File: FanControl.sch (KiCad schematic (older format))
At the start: 4 parts

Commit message: Finish the schematics. All pins are assinged to the NUCLEO-64 board.
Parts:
- gave numbers to parts that had none: 4
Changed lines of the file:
@@
 $EndDescr
 $Comp
-L Device:R R?
+L Device:R R51
 U 1 1 5AB90282
 P 4500 3500
-AR Path="/5AB9002A/5AB90282" Ref="R?"  Part="1"
-AR Path="/5AB91A71/5AB90282" Ref="R?"  Part="1"
-F 0 "R?" V 4293 3500 50  0000 C CNN
+AR Path="/5AB9002A/5AB90282" Ref="R51"  Part="1"
+AR Path="/5AB91A5D/5AB90282" Ref="R53"  Part="1"
+AR Path="/5AB91A68/5AB90282" Ref="R55"  Part="1"
+AR Path="/5AB91A71/5AB90282" Ref="R57"  Part="1"
+F 0 "R57" V 4293 3500 50  0000 C CNN
 F 1 "1k" V 4384 3500 50  0000 C CNN
 F 2 "" V 4430 3500 50  0001 C CNN
@@
 $EndComp
 $Comp
-L power:GND #PWR?
+L power:GND #PWR071
 U 1 1 5AB906E9
 P 5250 4000
-AR Path="/5AB9002A/5AB906E9" Ref="#PWR?"  Part="1"
-AR Path="/5AB91A71/5AB906E9" Ref="#PWR?"  Part="1"
-F 0 "#PWR?" H 5250 3750 50  0001 C CNN
+AR Path="/5AB9002A/5AB906E9" Ref="#PWR071"  Part="1"
+AR Path="/5AB91A5D/5AB906E9" Ref="#PWR072"  Part="1"
+AR Path="/5AB91A68/5AB906E9" Ref="#PWR073"  Part="1"
+AR Path="/5AB91A71/5AB906E9" Ref="#PWR074"  Part="1"
+F 0 "#PWR074" H 5250 3750 50  0001 C CNN
 F 1 "GND" H 5255 3827 50  0000 C CNN
 F 2 "" H 5250 4000 50  0001 C CNN
@@
 V_FAN
 $Comp
-L bsh105:BSH105 TR?
+L bsh105:BSH105 TR4
 U 1 1 5AB90621
 P 5100 3500
-AR Path="/5AB9002A/5AB90621" Ref="TR?"  Part="1"
-AR Path="/5AB91A71/5AB90621" Ref="TR?"  Part="1"
-F 0 "TR?" H 5328 3553 70  0000 L CNN
+AR Path="/5AB9002A/5AB90621" Ref="TR4"  Part="1"
+AR Path="/5AB91A5D/5AB90621" Ref="TR5"  Part="1"
+AR Path="/5AB91A68/5AB90621" Ref="TR6"  Part="1"
+AR Path="/5AB91A71/5AB90621" Ref="TR7"  Part="1"
+F 0 "TR7" H 5328 3553 70  0000 L CNN
 F 1 "PMV40UN2" H 5328 3439 60  0000 L CNN
 F 2 "" H 5100 3500 60  0000 C CNN
@@
 	5250 2700 5250 3150
 $Comp
-L Device:R R?
+L Device:R R50
 U 1 1 5AB969B0
 P 4250 3750
-F 0 "R?" H 4320 3796 50  0000 L CNN
+AR Path="/5AB9002A/5AB969B0" Ref="R50"  Part="1"
+AR Path="/5AB91A5D/5AB969B0" Ref="R52"  Part="1"
+AR Path="/5AB91A68/5AB969B0" Ref="R54"  Part="1"
+AR Path="/5AB91A71/5AB969B0" Ref="R56"  Part="1"
+F 0 "R56" H 4320 3796 50  0000 L CNN
 F 1 "10k" H 4320 3705 50  0000 L CNN
 F 2 "" V 4180 3750 50  0001 C CNN
@@
 	5250 3950 5250 4000
 $Comp
-L Device:D D?
+L Device:D D12
 U 1 1 5AB96AD6
 P 5250 2450
-F 0 "D?" V 5204 2529 50  0000 L CNN
+AR Path="/5AB9002A/5AB96AD6" Ref="D12"  Part="1"
+AR Path="/5AB91A5D/5AB96AD6" Ref="D13"  Part="1"
+AR Path="/5AB91A68/5AB96AD6" Ref="D14"  Part="1"
+AR Path="/5AB91A71/5AB96AD6" Ref="D15"  Part="1"
+F 0 "D15" V 5204 2529 50  0000 L CNN
 F 1 "DO-219AB" V 5295 2529 50  0000 L CNN
 F 2 "" H 5250 2450 50  0001 C CNN

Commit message: Split the bed heater in separate schematics.
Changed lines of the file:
@@
 $Descr A4 11693 8268
 encoding utf-8
-Sheet 34 35
+Sheet 31 35
 Title ""
 Date ""
@@
 AR Path="/5AB91A68/5AB90282" Ref="R55"  Part="1"
 AR Path="/5AB91A71/5AB90282" Ref="R57"  Part="1"
-F 0 "R57" V 4293 3500 50  0000 C CNN
+F 0 "R51" V 4293 3500 50  0000 C CNN
 F 1 "1k" V 4384 3500 50  0000 C CNN
 F 2 "" V 4430 3500 50  0001 C CNN
@@
 AR Path="/5AB91A68/5AB90621" Ref="TR6"  Part="1"
 AR Path="/5AB91A71/5AB90621" Ref="TR7"  Part="1"
-F 0 "TR7" H 5328 3553 70  0000 L CNN
+F 0 "TR4" H 5328 3553 70  0000 L CNN
 F 1 "PMV40UN2" H 5328 3439 60  0000 L CNN
 F 2 "" H 5100 3500 60  0000 C CNN
@@
 AR Path="/5AB91A68/5AB969B0" Ref="R54"  Part="1"
 AR Path="/5AB91A71/5AB969B0" Ref="R56"  Part="1"
-F 0 "R56" H 4320 3796 50  0000 L CNN
+F 0 "R50" H 4320 3796 50  0000 L CNN
 F 1 "10k" H 4320 3705 50  0000 L CNN
 F 2 "" V 4180 3750 50  0001 C CNN
@@
 AR Path="/5AB91A68/5AB96AD6" Ref="D14"  Part="1"
 AR Path="/5AB91A71/5AB96AD6" Ref="D15"  Part="1"
-F 0 "D15" V 5204 2529 50  0000 L CNN
+F 0 "D12" V 5204 2529 50  0000 L CNN
 F 1 "DO-219AB" V 5295 2529 50  0000 L CNN
 F 2 "" H 5250 2450 50  0001 C CNN

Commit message: Assigned footprints for all components. Inductors are approximate size. MOSFETs dont agree with the footprints. Saved pcb netlist report as report.txt.
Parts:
- D12: footprint (none) -> Diode_SMD:D_SOD-323F
- R50, R51: footprint (none) -> Resistor_SMD:R_0603_1608Metric
- TR4: value PMV40UN2 -> SI2318CDS; footprint (none) -> Package_TO_SOT_SMD:SOT-23
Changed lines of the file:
@@
 AR Path="/5AB91A68/5AB90282" Ref="R55"  Part="1"
 AR Path="/5AB91A71/5AB90282" Ref="R57"  Part="1"
-F 0 "R51" V 4293 3500 50  0000 C CNN
+F 0 "R57" V 4293 3500 50  0000 C CNN
 F 1 "1k" V 4384 3500 50  0000 C CNN
-F 2 "" V 4430 3500 50  0001 C CNN
+F 2 "Resistor_SMD:R_0603_1608Metric" V 4430 3500 50  0001 C CNN
 F 3 "~" H 4500 3500 50  0001 C CNN
 	1    4500 3500
@@
 AR Path="/5AB91A68/5AB90621" Ref="TR6"  Part="1"
 AR Path="/5AB91A71/5AB90621" Ref="TR7"  Part="1"
-F 0 "TR4" H 5328 3553 70  0000 L CNN
-F 1 "PMV40UN2" H 5328 3439 60  0000 L CNN
-F 2 "" H 5100 3500 60  0000 C CNN
+F 0 "TR7" H 5328 3553 70  0000 L CNN
+F 1 "SI2318CDS" H 5328 3439 60  0000 L CNN
+F 2 "Package_TO_SOT_SMD:SOT-23" H 5100 3500 60  0001 C CNN
 F 3 "" H 5100 3500 60  0000 C CNN
 	1    5100 3500
@@
 AR Path="/5AB91A68/5AB969B0" Ref="R54"  Part="1"
 AR Path="/5AB91A71/5AB969B0" Ref="R56"  Part="1"
-F 0 "R50" H 4320 3796 50  0000 L CNN
+F 0 "R56" H 4320 3796 50  0000 L CNN
 F 1 "10k" H 4320 3705 50  0000 L CNN
-F 2 "" V 4180 3750 50  0001 C CNN
+F 2 "Resistor_SMD:R_0603_1608Metric" V 4180 3750 50  0001 C CNN
 F 3 "~" H 4250 3750 50  0001 C CNN
 	1    4250 3750
@@
 AR Path="/5AB91A68/5AB96AD6" Ref="D14"  Part="1"
 AR Path="/5AB91A71/5AB96AD6" Ref="D15"  Part="1"
-F 0 "D12" V 5204 2529 50  0000 L CNN
+F 0 "D15" V 5204 2529 50  0000 L CNN
 F 1 "DO-219AB" V 5295 2529 50  0000 L CNN
-F 2 "" H 5250 2450 50  0001 C CNN
+F 2 "Diode_SMD:D_SOD-323F" H 5250 2450 50  0001 C CNN
 F 3 "~" H 5250 2450 50  0001 C CNN
 	1    5250 2450

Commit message: Updated components. Removed power supply. Component layout on PCB.
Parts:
- TR4: footprint Package_TO_SOT_SMD:SOT-23 -> PrntrBoardV1:SOT-23
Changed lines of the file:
@@
 $Descr A4 11693 8268
 encoding utf-8
-Sheet 31 35
+Sheet 31 34
 Title ""
 Date ""
@@
 AR Path="/5AB91A68/5AB90282" Ref="R55"  Part="1"
 AR Path="/5AB91A71/5AB90282" Ref="R57"  Part="1"
-F 0 "R57" V 4293 3500 50  0000 C CNN
+F 0 "R51" V 4293 3500 50  0000 C CNN
 F 1 "1k" V 4384 3500 50  0000 C CNN
 F 2 "Resistor_SMD:R_0603_1608Metric" V 4430 3500 50  0001 C CNN
@@
 AR Path="/5AB91A68/5AB90621" Ref="TR6"  Part="1"
 AR Path="/5AB91A71/5AB90621" Ref="TR7"  Part="1"
-F 0 "TR7" H 5328 3553 70  0000 L CNN
+F 0 "TR4" H 5328 3553 70  0000 L CNN
 F 1 "SI2318CDS" H 5328 3439 60  0000 L CNN
-F 2 "Package_TO_SOT_SMD:SOT-23" H 5100 3500 60  0001 C CNN
+F 2 "PrntrBoardV1:SOT-23" H 5100 3500 60  0001 C CNN
 F 3 "" H 5100 3500 60  0000 C CNN
 	1    5100 3500
@@
 AR Path="/5AB91A68/5AB969B0" Ref="R54"  Part="1"
 AR Path="/5AB91A71/5AB969B0" Ref="R56"  Part="1"
-F 0 "R56" H 4320 3796 50  0000 L CNN
+F 0 "R50" H 4320 3796 50  0000 L CNN
 F 1 "10k" H 4320 3705 50  0000 L CNN
 F 2 "Resistor_SMD:R_0603_1608Metric" V 4180 3750 50  0001 C CNN
@@
 AR Path="/5AB91A68/5AB96AD6" Ref="D14"  Part="1"
 AR Path="/5AB91A71/5AB96AD6" Ref="D15"  Part="1"
-F 0 "D15" V 5204 2529 50  0000 L CNN
+F 0 "D12" V 5204 2529 50  0000 L CNN
 F 1 "DO-219AB" V 5295 2529 50  0000 L CNN
 F 2 "Diode_SMD:D_SOD-323F" H 5250 2450 50  0001 C CNN

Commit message: Routed most of the power traces.
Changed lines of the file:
@@
 AR Path="/5AB91A68/5AB90282" Ref="R55"  Part="1"
 AR Path="/5AB91A71/5AB90282" Ref="R57"  Part="1"
-F 0 "R51" V 4293 3500 50  0000 C CNN
+F 0 "R57" V 4293 3500 50  0000 C CNN
 F 1 "1k" V 4384 3500 50  0000 C CNN
 F 2 "Resistor_SMD:R_0603_1608Metric" V 4430 3500 50  0001 C CNN
@@
 AR Path="/5AB91A68/5AB90621" Ref="TR6"  Part="1"
 AR Path="/5AB91A71/5AB90621" Ref="TR7"  Part="1"
-F 0 "TR4" H 5328 3553 70  0000 L CNN
+F 0 "TR7" H 5328 3553 70  0000 L CNN
 F 1 "SI2318CDS" H 5328 3439 60  0000 L CNN
 F 2 "PrntrBoardV1:SOT-23" H 5100 3500 60  0001 C CNN
@@
 AR Path="/5AB91A68/5AB969B0" Ref="R54"  Part="1"
 AR Path="/5AB91A71/5AB969B0" Ref="R56"  Part="1"
-F 0 "R50" H 4320 3796 50  0000 L CNN
+F 0 "R56" H 4320 3796 50  0000 L CNN
 F 1 "10k" H 4320 3705 50  0000 L CNN
 F 2 "Resistor_SMD:R_0603_1608Metric" V 4180 3750 50  0001 C CNN
@@
 AR Path="/5AB91A68/5AB96AD6" Ref="D14"  Part="1"
 AR Path="/5AB91A71/5AB96AD6" Ref="D15"  Part="1"
-F 0 "D12" V 5204 2529 50  0000 L CNN
+F 0 "D15" V 5204 2529 50  0000 L CNN
 F 1 "DO-219AB" V 5295 2529 50  0000 L CNN
 F 2 "Diode_SMD:D_SOD-323F" H 5250 2450 50  0001 C CNN

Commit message: Added mounting holes and fiducials. Placed all components labels so they are readable.
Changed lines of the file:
@@
 AR Path="/5AB91A68/5AB90282" Ref="R55"  Part="1"
 AR Path="/5AB91A71/5AB90282" Ref="R57"  Part="1"
-F 0 "R57" V 4293 3500 50  0000 C CNN
+F 0 "R51" V 4293 3500 50  0000 C CNN
 F 1 "1k" V 4384 3500 50  0000 C CNN
 F 2 "Resistor_SMD:R_0603_1608Metric" V 4430 3500 50  0001 C CNN
@@
 AR Path="/5AB91A68/5AB90621" Ref="TR6"  Part="1"
 AR Path="/5AB91A71/5AB90621" Ref="TR7"  Part="1"
-F 0 "TR7" H 5328 3553 70  0000 L CNN
+F 0 "TR4" H 5328 3553 70  0000 L CNN
 F 1 "SI2318CDS" H 5328 3439 60  0000 L CNN
 F 2 "PrntrBoardV1:SOT-23" H 5100 3500 60  0001 C CNN
@@
 AR Path="/5AB91A68/5AB969B0" Ref="R54"  Part="1"
 AR Path="/5AB91A71/5AB969B0" Ref="R56"  Part="1"
-F 0 "R56" H 4320 3796 50  0000 L CNN
+F 0 "R50" H 4320 3796 50  0000 L CNN
 F 1 "10k" H 4320 3705 50  0000 L CNN
 F 2 "Resistor_SMD:R_0603_1608Metric" V 4180 3750 50  0001 C CNN
@@
 AR Path="/5AB91A68/5AB96AD6" Ref="D14"  Part="1"
 AR Path="/5AB91A71/5AB96AD6" Ref="D15"  Part="1"
-F 0 "D15" V 5204 2529 50  0000 L CNN
+F 0 "D12" V 5204 2529 50  0000 L CNN
 F 1 "DO-219AB" V 5295 2529 50  0000 L CNN
 F 2 "Diode_SMD:D_SOD-323F" H 5250 2450 50  0001 C CNN

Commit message: Update schematics to use TMC5130/TMC2130 drivers.
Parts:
- D12: value DO-219AB -> 1N4148
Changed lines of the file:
@@
 AR Path="/5AB91A68/5AB90282" Ref="R55"  Part="1"
 AR Path="/5AB91A71/5AB90282" Ref="R57"  Part="1"
-F 0 "R51" V 4293 3500 50  0000 C CNN
+F 0 "R57" V 4293 3500 50  0000 C CNN
 F 1 "1k" V 4384 3500 50  0000 C CNN
 F 2 "Resistor_SMD:R_0603_1608Metric" V 4430 3500 50  0001 C CNN
@@
 AR Path="/5AB91A68/5AB90621" Ref="TR6"  Part="1"
 AR Path="/5AB91A71/5AB90621" Ref="TR7"  Part="1"
-F 0 "TR4" H 5328 3553 70  0000 L CNN
+F 0 "TR7" H 5328 3553 70  0000 L CNN
 F 1 "SI2318CDS" H 5328 3439 60  0000 L CNN
 F 2 "PrntrBoardV1:SOT-23" H 5100 3500 60  0001 C CNN
@@
 AR Path="/5AB91A68/5AB969B0" Ref="R54"  Part="1"
 AR Path="/5AB91A71/5AB969B0" Ref="R56"  Part="1"
-F 0 "R50" H 4320 3796 50  0000 L CNN
+F 0 "R56" H 4320 3796 50  0000 L CNN
 F 1 "10k" H 4320 3705 50  0000 L CNN
 F 2 "Resistor_SMD:R_0603_1608Metric" V 4180 3750 50  0001 C CNN
@@
 AR Path="/5AB91A68/5AB96AD6" Ref="D14"  Part="1"
 AR Path="/5AB91A71/5AB96AD6" Ref="D15"  Part="1"
-F 0 "D12" V 5204 2529 50  0000 L CNN
-F 1 "DO-219AB" V 5295 2529 50  0000 L CNN
+F 0 "D15" V 5204 2529 50  0000 L CNN
+F 1 "1N4148" V 5295 2529 50  0000 L CNN
 F 2 "Diode_SMD:D_SOD-323F" H 5250 2450 50  0001 C CNN
 F 3 "~" H 5250 2450 50  0001 C CNN

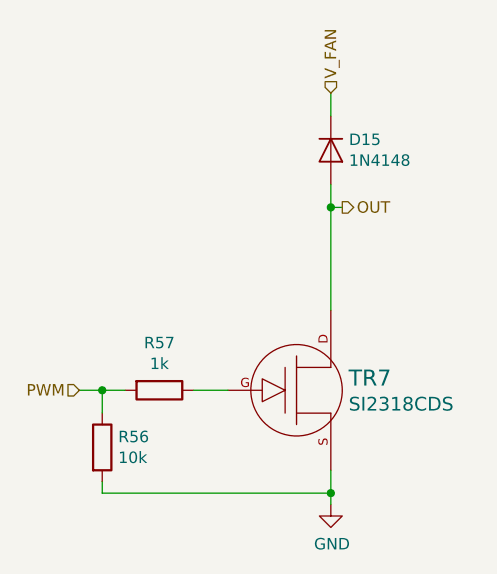
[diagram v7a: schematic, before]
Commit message: Switched to local foorprints for terminals and LED. Switched to local foorprint for the printer driver ship - it has larger thermal pad ares.
Placement V1 complete.
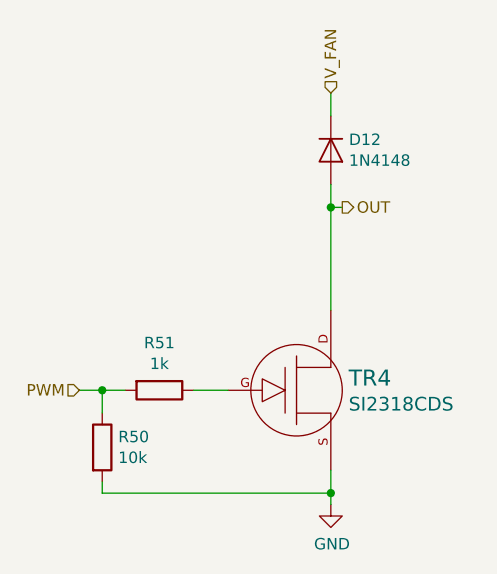
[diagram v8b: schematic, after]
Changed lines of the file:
@@
 AR Path="/5AB91A68/5AB90282" Ref="R55"  Part="1"
 AR Path="/5AB91A71/5AB90282" Ref="R57"  Part="1"
-F 0 "R57" V 4293 3500 50  0000 C CNN
+F 0 "R51" V 4293 3500 50  0000 C CNN
 F 1 "1k" V 4384 3500 50  0000 C CNN
 F 2 "Resistor_SMD:R_0603_1608Metric" V 4430 3500 50  0001 C CNN
@@
 AR Path="/5AB91A68/5AB906E9" Ref="#PWR073"  Part="1"
 AR Path="/5AB91A71/5AB906E9" Ref="#PWR074"  Part="1"
-F 0 "#PWR074" H 5250 3750 50  0001 C CNN
+F 0 "#PWR071" H 5250 3750 50  0001 C CNN
 F 1 "GND" H 5255 3827 50  0000 C CNN
 F 2 "" H 5250 4000 50  0001 C CNN
@@
 AR Path="/5AB91A68/5AB90621" Ref="TR6"  Part="1"
 AR Path="/5AB91A71/5AB90621" Ref="TR7"  Part="1"
-F 0 "TR7" H 5328 3553 70  0000 L CNN
+F 0 "TR4" H 5328 3553 70  0000 L CNN
 F 1 "SI2318CDS" H 5328 3439 60  0000 L CNN
 F 2 "PrntrBoardV1:SOT-23" H 5100 3500 60  0001 C CNN
@@
 AR Path="/5AB91A68/5AB969B0" Ref="R54"  Part="1"
 AR Path="/5AB91A71/5AB969B0" Ref="R56"  Part="1"
-F 0 "R56" H 4320 3796 50  0000 L CNN
+F 0 "R50" H 4320 3796 50  0000 L CNN
 F 1 "10k" H 4320 3705 50  0000 L CNN
 F 2 "Resistor_SMD:R_0603_1608Metric" V 4180 3750 50  0001 C CNN
@@
 AR Path="/5AB91A68/5AB96AD6" Ref="D14"  Part="1"
 AR Path="/5AB91A71/5AB96AD6" Ref="D15"  Part="1"
-F 0 "D15" V 5204 2529 50  0000 L CNN
+F 0 "D12" V 5204 2529 50  0000 L CNN
 F 1 "1N4148" V 5295 2529 50  0000 L CNN
 F 2 "Diode_SMD:D_SOD-323F" H 5250 2450 50  0001 C CNN
